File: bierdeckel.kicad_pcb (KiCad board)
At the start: 2 copper layers, 93 x 93 mm, 90 parts, among them IC1 HSFPAR004A, J1 Pogo, J2 Pogo, J3 Pogo, J4 Pogo, Q1 BSS138P,215, SW1 PTS526 SK15 SMTR2 LFS, SW2 PTS526 SK15 SMTR2 LFS, SW3 PTS526 SK15 SMTR2 LFS, U1 ESP32-C3-WROOM-02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

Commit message: continue routing
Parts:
- added C30: 0.1uF, Capacitor_SMD:C_0805_2012Metric, F.Cu at (108.3, 130.5)
- moved C25 8.63 mm to (149.8, 74.2), turned to 180 degrees
- moved C7 3.71 mm to (108.7, 134.3), turned to -45 degrees
- moved R18 3.49 mm to (148.0, 62.3), turned to -90 degrees
- moved C6 2.64 mm to (184.4, 134.4), turned to -135 degrees
- moved IC1 2.33 mm to (111.1, 131.9)
- moved R27 2.20 mm to (114.8, 123.4)
- moved R28 1.69 mm to (114.0, 120.6), turned to 180 degrees
- moved B3 1.68 mm to (111.7, 58.3)
- moved C27 1.44 mm to (110.5, 120.6), turned to 180 degrees
- moved C8 1.39 mm to (108.5, 60.2)
- moved B2 1.11 mm to (177.1, 58.0)
- moved C5 1.03 mm to (184.3, 58.6), turned to 135 degrees
- moved TP2 0.67 mm to (148.8, 77.5)
- moved B4 0.65 mm to (140.2, 69.7)
- moved B5 0.65 mm to (149.6, 69.0)
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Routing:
- net /Vpress: track 24.8 -> 61.5 mm
- net +3.3V: track 320.9 -> 295.3 mm
- net /Pressure Gauge/VR+: track 3.27 -> 6.35 mm
- net Net-(D4-DOUT): track 81.4 -> 78.6 mm
- net GND: track 68.6 -> 70.8 mm
- net Net-(U4-BAT): track 0.00 -> 1.87 mm
- net Net-(D3-DOUT): track 83.7 -> 81.9 mm
- net +BATT: track 92.9 -> 94.7 mm
- net /Pressure Gauge/VR-: track 3.29 -> 4.78 mm
- net Net-(D2-DOUT): track 78.0 -> 78.8 mm
- net Net-(D1-DOUT): track 76.2 -> 76.7 mm
- added copper zone on F.Cu, net Net-(U4-BAT)

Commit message: continue refactor
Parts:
- removed TP4, TP7: TestPoint, TestPoint:TestPoint_Pad_D1.0mm
- moved C30 72.1 mm to (112.3, 58.5), turned to 0 degrees
- moved IC1 70.7 mm to (111.1, 61.1), turned to -45 degrees
- moved R21 63.6 mm to (114.4, 61.5), turned to 180 degrees
- moved R27 59.4 mm to (108.9, 64.3), turned to 90 degrees
- moved U6 59.2 mm to (111.8, 65.7), turned to -90 degrees
- moved R28 52.9 mm to (108.9, 67.9), turned to -90 degrees
- moved C27 50.7 mm to (111.7, 69.9), turned to 0 degrees
- moved B3 15.3 mm to (96.4, 58.1)
- moved C2 11.9 mm to (109.4, 72.8), turned to -90 degrees
- moved SW2 9.65 mm to (111.9, 79.4)
- moved C1 9.65 mm to (110.2, 75.6)
- moved R7 9.65 mm to (113.7, 75.6)
- moved SW3 8.15 mm to (111.9, 85.5)
- moved C8 1.60 mm to (108.6, 58.6), turned to 45 degrees
- moved C3 0.75 mm to (115.2, 64.2), turned to 90 degrees
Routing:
- net /Vpress: track 61.5 -> 0.00 mm
- net /~{BOOTLOADER}: track 2.45 -> 16.6 mm
- net /RST: track 13.4 -> 24.6 mm
- net +3.3V: track 295.3 -> 302.2 mm
- net Net-(U6-RG__1): track 2.29 -> 7.41 mm
- net /Pressure Gauge/VR+: track 6.35 -> 3.00 mm
- net /Pressure Gauge/VR-: track 4.78 -> 2.49 mm

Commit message: further work
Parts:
- added C31: 0.1uF, Capacitor_SMD:C_0603_1608Metric, F.Cu at (110.9, 76.3)
- added R22: 4k, Resistor_SMD:R_0603_1608Metric, F.Cu at (108.5, 75.5)
- C13, C27, C3, C30, C4, C5, C6, C7, C8: footprint Capacitor_SMD:C_0805_2012Metric -> Capacitor_SMD:C_0603_1608Metric
- R1, R10, R11, R12, R13, R14, R16, R18, R2, R21, R27, R28, R3, R4, R5, R6, R7, R8, R9: footprint Resistor_SMD:R_0805_2012Metric -> Resistor_SMD:R_0603_1608Metric
- moved SW2 10.9 mm to (109.9, 90.1), turned to -90 degrees
- moved R7 10.7 mm to (108.6, 85.1), turned to 0 degrees
- moved C1 9.58 mm to (112.1, 85.0), turned to 0 degrees
- moved R21 8.55 mm to (112.8, 69.9), turned to 90 degrees
- moved B3 7.75 mm to (94.9, 65.7)
- moved SW3 6.16 mm to (116.0, 90.1), turned to -90 degrees
- moved R27 5.58 mm to (107.7, 69.8)
- moved C2 5.54 mm to (113.7, 76.3)
- moved R28 4.99 mm to (107.7, 72.8)
- moved U6 4.45 mm to (110.3, 69.9)
- moved C27 4.14 mm to (110.5, 73.8)
- moved C3 0.41 mm to (115.5, 64.5)
- moved C10 0.28 mm to (131.5, 91.2)
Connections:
- U6 pad 6: /Vpress -> Net-(U6-VOUT)
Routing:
- net /Vpress: track 0.00 -> 7.85 mm
- net Net-(U6-VOUT): track 0.00 -> 6.85 mm
- net Net-(U6-RG__1): track 7.41 -> 2.07 mm
- net /Pressure Gauge/VR-: track 2.49 -> 7.27 mm
- net /Pressure Gauge/VR+: track 3.00 -> 6.64 mm
- net +3.3V: track 302.2 -> 305.6 mm
- net /~{BOOTLOADER}: track 16.6 -> 18.9 mm
- net /Pressure Gauge/Vref: track 4.03 -> 3.00 mm
- net /RST: track 24.6 -> 25.1 mm

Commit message: before USB connector
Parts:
- added J6: USB4110-GF-A, Connector_USB:USB_C_Receptacle_GCT_USB4110, F.Cu at (141.6, 49.9)
- added R23: 5k1, Resistor_SMD:R_0603_1608Metric, F.Cu at (146.8, 44.0)
- added R24: 5k1, Resistor_SMD:R_0603_1608Metric, F.Cu at (146.8, 41.5)
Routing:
- net /USB-: track 17.1 -> 19.3 mm
- net /USB+: track 15.9 -> 18.1 mm

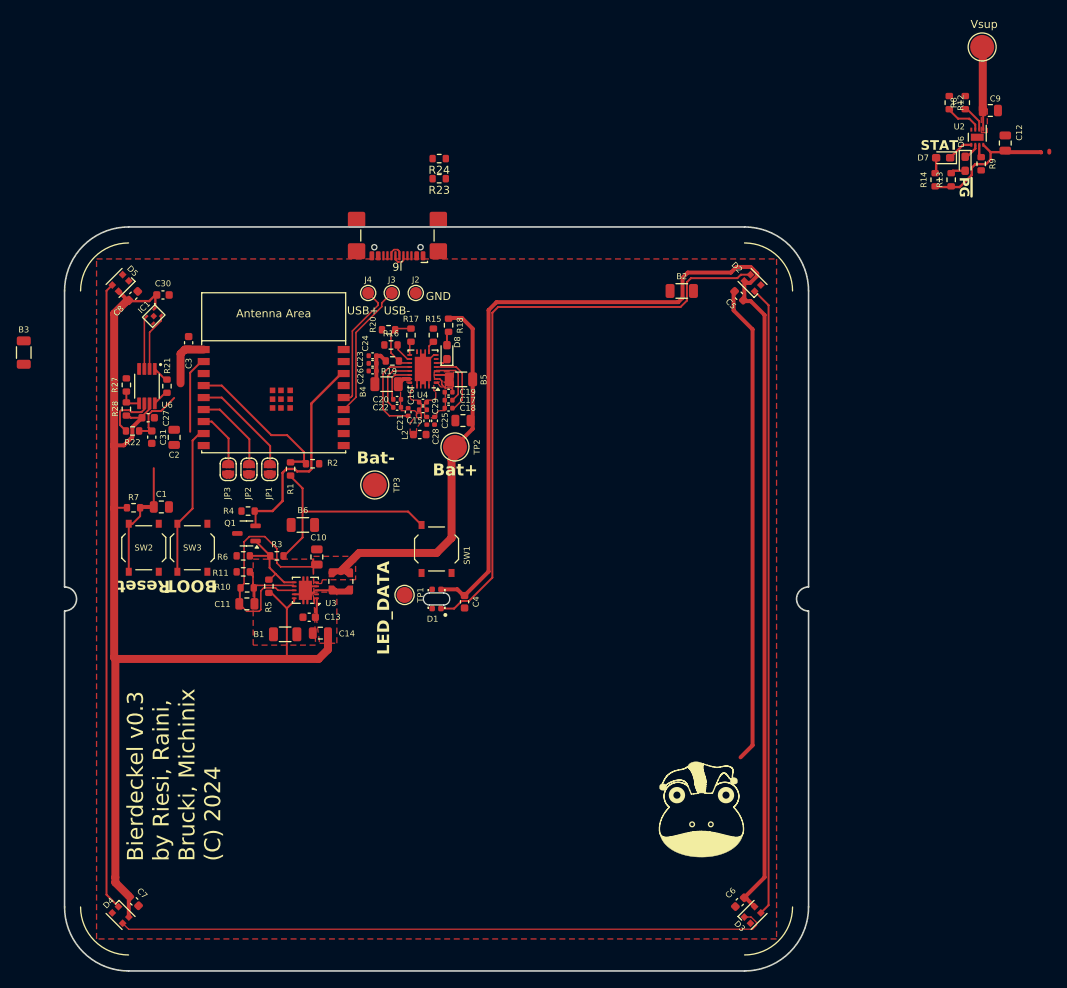
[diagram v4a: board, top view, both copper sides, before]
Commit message: add usb c connector
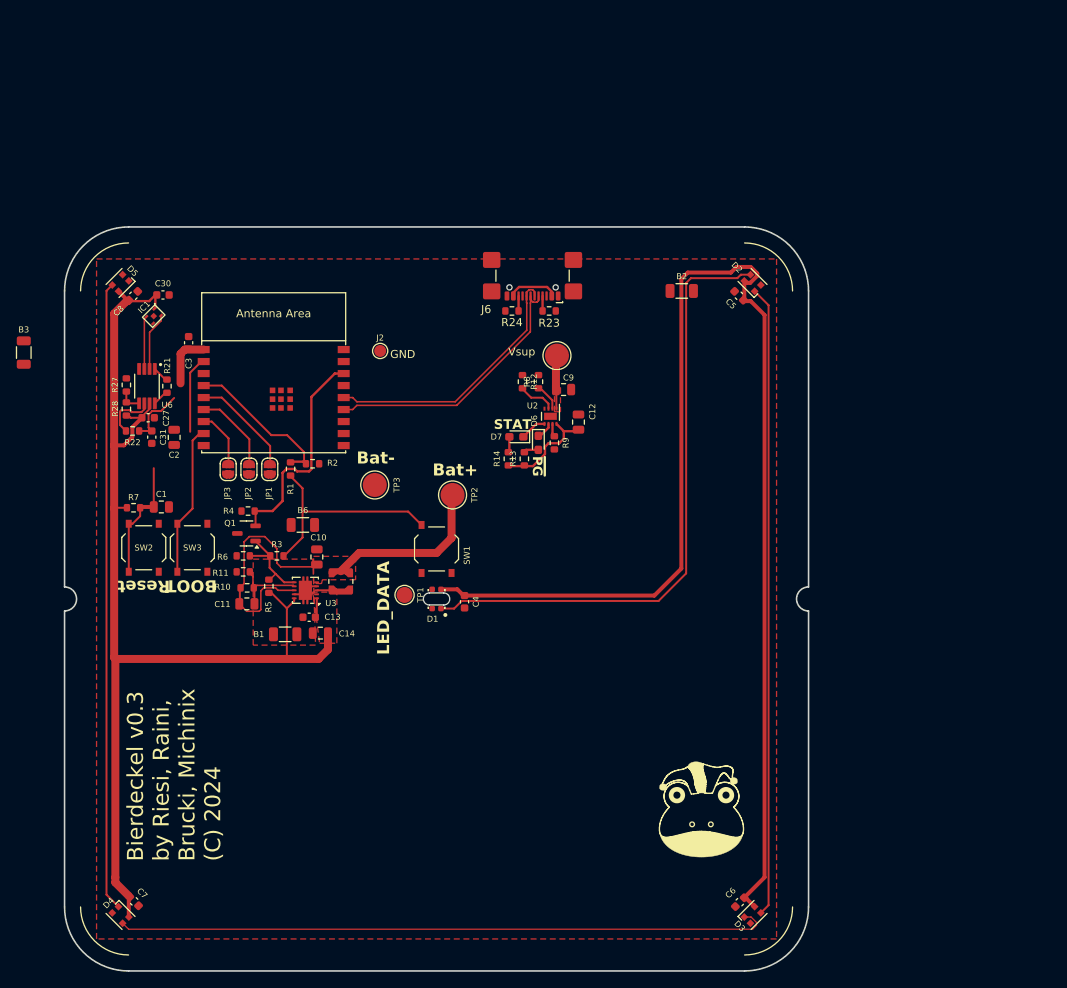
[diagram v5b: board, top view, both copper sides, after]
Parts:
- removed B4, B5: 0R, Resistor_SMD:R_1206_3216Metric
- removed C15, C28: 56nF, Capacitor_SMD:C_0402_1005Metric
- removed C16, C29: 820pF, Capacitor_SMD:C_0402_1005Metric
- removed C17, C22: 470nF 25V, Capacitor_SMD:C_0402_1005Metric
- removed C18, C21: 22nF 25V, Capacitor_SMD:C_0402_1005Metric
- removed C19, C20: 10nF 25V, Capacitor_SMD:C_0402_1005Metric
- removed C23, C24: 10uF 25V, Capacitor_SMD:C_0402_1005Metric
- removed C25: 1uF, Capacitor_SMD:C_0805_2012Metric
- removed C26: 0.1uF 25V, Capacitor_SMD:C_0402_1005Metric
- removed D8: 150060GS73220, LED_SMD:LED_0603_1608Metric_Pad1.05x0.95mm_HandSolder
- removed J3, J4: Pogo, TestPoint:TestPoint_Pad_D1.5mm
- removed L2: 8.3uH 160mOhm, Inductor_SMD:L_0603_1608Metric
- removed R15: 2k4, Resistor_SMD:R_0603_1608Metric
- removed R16, R18: 10k, Resistor_SMD:R_0603_1608Metric
- removed R17: 330, Resistor_SMD:R_0603_1608Metric
- removed R19: 42k, Resistor_SMD:R_0603_1608Metric
- removed R20: 300, Resistor_SMD:R_0603_1608Metric
- removed U4: BQ51050BRHL, Package_DFN_QFN:Texas_VQFN-RHL-20
- moved J1 65.7 mm to (161.5, 66.1)
- moved U2 63.7 mm to (160.7, 73.7)
- moved C12 63.7 mm to (164.2, 74.4)
- moved C9 63.7 mm to (162.4, 70.3)
- moved D6 63.7 mm to (159.2, 77.0)
- moved D7 63.7 mm to (156.5, 76.2)
- moved R12 63.7 mm to (157.2, 69.3)
- moved R13 63.7 mm to (157.5, 79.0)
- moved R14 63.7 mm to (155.5, 79.0)
- moved R8 63.7 mm to (159.2, 69.3)
- moved R9 63.7 mm to (161.2, 77.0)
- moved R23 21.5 mm to (160.6, 60.5), turned to 0 degrees
- moved R24 21.1 mm to (155.9, 60.5)
- moved J6 17.6 mm to (158.5, 54.9)
- moved J2 8.51 mm to (139.4, 65.5)
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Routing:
- net GND: track 70.8 -> 3.31 mm
- net +BATT: track 94.5 -> 64.0 mm
- net /USB+: track 18.1 -> 33.3 mm
- net /USB-: track 19.3 -> 34.1 mm
- net Net-(U4-COMM2): track 11.6 -> 0.00 mm
- net Net-(U4-COMM1): track 8.59 -> 0.00 mm
- net Net-(U4-FOD): track 8.02 -> 0.00 mm
- net Net-(U4-CLAMP2): track 7.21 -> 0.00 mm
- net Net-(U4-CLAMP1): track 6.56 -> 0.00 mm
- net Net-(U4-BOOT2): track 5.12 -> 0.00 mm
- net Net-(B4-Pad2): track 5.07 -> 0.00 mm
- net Net-(U4-BOOT1): track 3.28 -> 0.00 mm
- net /Vcharge: track 10.6 -> 13.3 mm
- net Net-(U4-TS/CTRL): track 2.52 -> 0.00 mm
- net Net-(J6-CC2): track 0.00 -> 1.87 mm
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- removed copper zone on F.Cu, net Net-(U4-AC1)
- removed copper zone on F.Cu, net Net-(U4-AC2)
- removed copper zone on F.Cu, net Net-(U4-BAT)
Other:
- board text removed: "USB+"
- board text removed: "USB-"

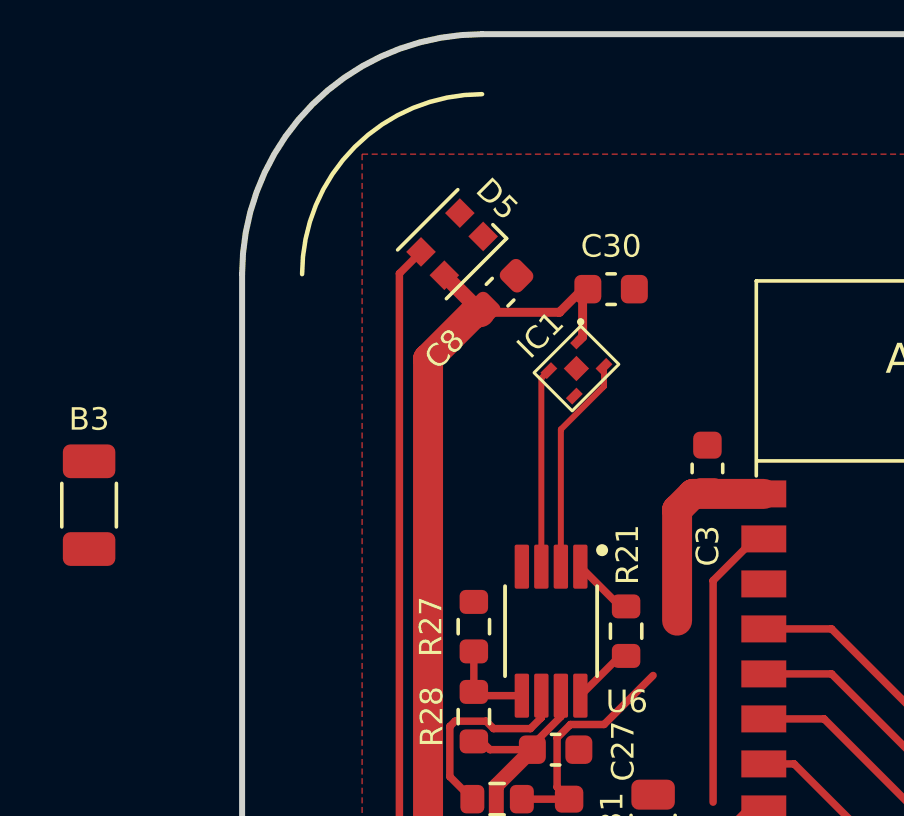
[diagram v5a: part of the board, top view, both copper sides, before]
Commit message: remove excessive ESP mini
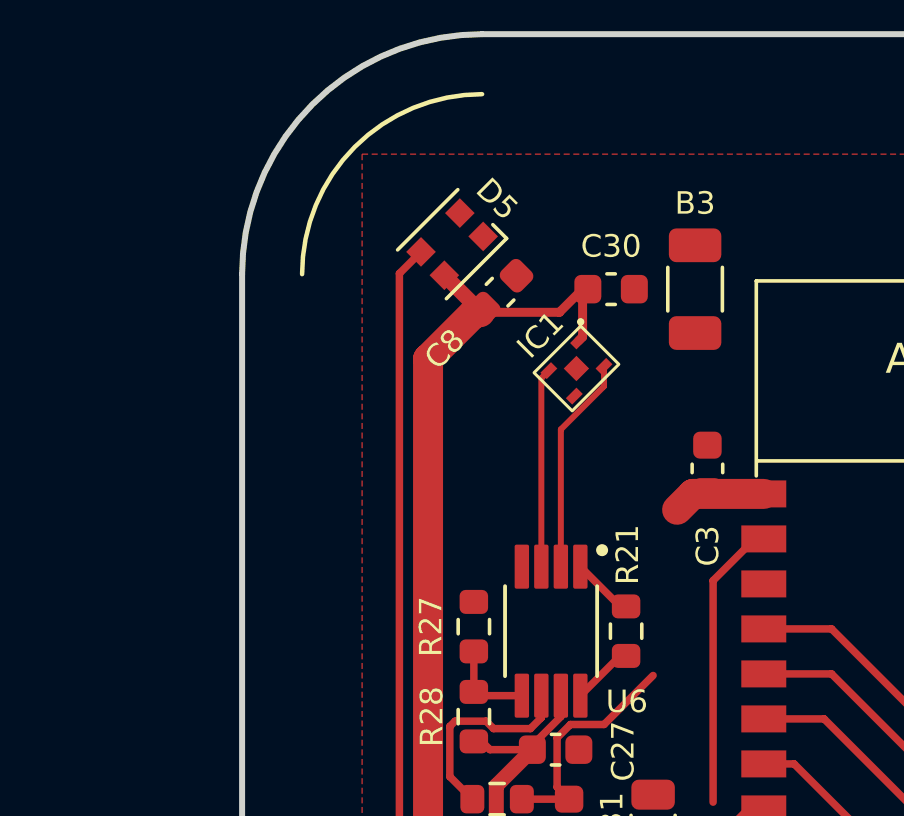
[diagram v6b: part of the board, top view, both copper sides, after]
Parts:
- moved B3 21.4 mm to (115.1, 58.5)
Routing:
- net +3.3V: track 306.2 -> 302.5 mm
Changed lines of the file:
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@@
 	(footprint "Resistor_SMD:R_1206_3216Metric"
 		(layer "F.Cu")
-		(at 94.9 65.7 -90)
+		(at 115.1 58.5 -90)
 		(descr "Resistor SMD 1206 (3216 Metric), square (rectangular) end terminal, IPC_7351 nominal, (Body size source: IPC-SM-782 page 72, https://www.pcb-3d.com/wordpress/wp-content/uploads/ipc-sm-782a_amendment_1_and_2.pdf), generated with kicad-footprint-generator")
 		(tags "resistor")
@@
 	)
 	(segment
-		(start 114.5 69.55)
-		(end 114.5 65.853748)
-		(width 1)
-		(layer "F.Cu")
-		(net 2)
-	)
-	(segment
 		(start 173.725 96.075)
 		(end 177.1 92.7)
@@
 			"d080d14a-b0cb-42f4-9839-25b9dda2cc1a" "d832029b-9f37-413b-a7ae-0f20db9cde78"
 			"dc85090e-04e8-4ee3-81e6-23dbbdc6f5c2" "e53f2e9a-951c-4d8f-98bc-b19d5fea81a5"
-			"ea633121-6b1c-4ca4-9539-7a4bd0b7e377" "efe2a5e6-6815-493c-a3cf-fc8b5dcee823"
-			"f68b30c1-1f82-45d7-a3d0-c7877e3d5d87" "fc7081c3-ab43-4d9d-bfea-540c2efae0ea"
-			"fe8c37be-36af-461d-b1cc-327ae24ce7f0"
+			"ea633121-6b1c-4ca4-9539-7a4bd0b7e377" "f68b30c1-1f82-45d7-a3d0-c7877e3d5d87"
+			"fc7081c3-ab43-4d9d-bfea-540c2efae0ea" "fe8c37be-36af-461d-b1cc-327ae24ce7f0"
 		)
 	)

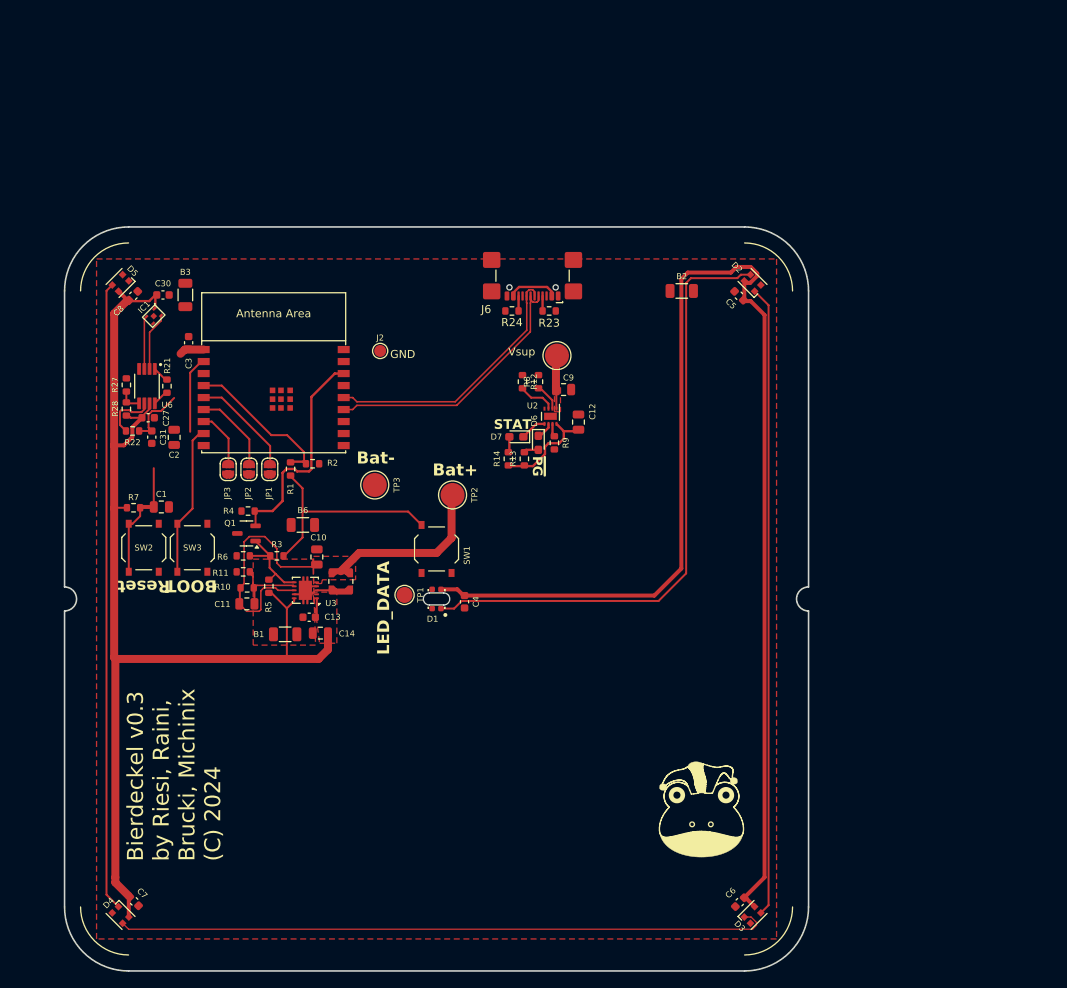
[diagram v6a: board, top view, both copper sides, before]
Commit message: finish up routing and fix latching
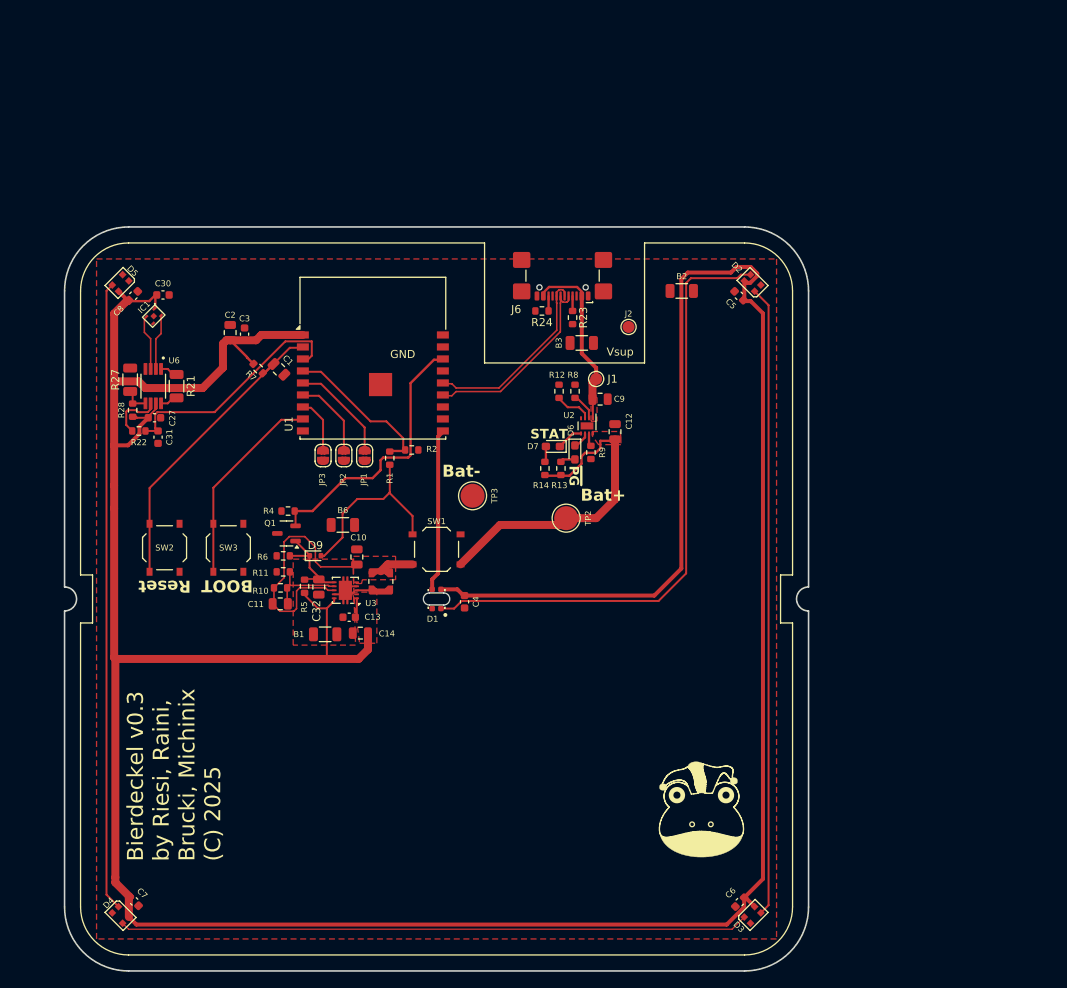
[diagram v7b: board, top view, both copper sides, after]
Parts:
- removed R3: 200k, Resistor_SMD:R_0603_1608Metric
- removed TP1: TestPoint, TestPoint:TestPoint_Pad_D2.0mm
- added C32: 1uF, Capacitor_SMD:C_0805_2012Metric, F.Cu at (131.8, 95.0)
- added D9: 1N4148WT, Diode_SMD:D_SOD-523, F.Cu at (131.3, 91.1)
- J1: footprint TestPoint:TestPoint_Pad_D3.0mm -> TestPoint:TestPoint_Pad_D1.5mm
- R21, R27: footprint Resistor_SMD:R_0603_1608Metric -> Resistor_SMD:R_1206_3216Metric
- U1: footprint PCM_Espressif:ESP32-C3-WROOM-02 -> RF_Module:ESP32-C3-WROOM-02
- moved B3 49.9 mm to (164.7, 64.5), turned to 0 degrees
- moved J2 31.2 mm to (170.5, 62.5)
- moved R7 23.4 mm to (124.2, 67.7), turned to -45 degrees
- moved C1 22.6 mm to (126.8, 67.8), turned to -45 degrees
- moved C2 14.9 mm to (120.7, 63.2), turned to 90 degrees
- moved TP2 14.5 mm to (162.7, 86.4)
- moved R2 12.5 mm to (143.4, 77.9)
- moved U1 12.5 mm to (138.5, 69.5)
- moved R1 12.5 mm to (140.7, 78.9)
- moved TP3 12.3 mm to (151.0, 83.6)
- moved JP2 12.0 mm to (134.9, 78.6)
- moved JP3 12.0 mm to (132.3, 78.6)
- moved JP1 12.0 mm to (137.5, 78.6)
- moved C3 7.07 mm to (122.5, 63.4)
- moved J1 5.70 mm to (166.4, 69.0)
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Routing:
- net +3.3V: track 302.5 -> 416.3 mm
- net /Vpress: track 7.85 -> 30.3 mm
- net /LED_DATA: track 0.00 -> 20.3 mm
- net /RST: track 25.1 -> 39.0 mm
- net +BATT: track 64.0 -> 77.3 mm
- net /Vcharge: track 13.3 -> 22.9 mm
- net /USB-: track 34.1 -> 24.7 mm
- net /USB+: track 33.3 -> 24.0 mm
- net /PWR_OFF: track 27.6 -> 34.1 mm
- net /~{BOOTLOADER}: track 18.9 -> 25.2 mm
- net Net-(D9-A): track 27.2 -> 23.5 mm
- net Net-(D3-DOUT): track 81.9 -> 78.6 mm
- net Net-(U3-UVLO): track 9.35 -> 10.5 mm
- net /PSU_EN: track 11.3 -> 12.3 mm
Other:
- board text added: "Bierdeckel v0.3 by Riesi, Raini, Brucki, Michinix (C) 2025"
- board text removed: "Bierdeckel v0.3 by Riesi, Raini, Brucki, Michinix (C) 2024"
- board text removed: "LED_DATA"
